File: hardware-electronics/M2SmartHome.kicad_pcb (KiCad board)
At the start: 4 copper layers, 22 x 76 mm, 208 parts, among them J1 M.2-Key-M-edge-connector, J3 CONMHF1-SMD-T, J4 CONMHF1-SMD-T, J5 Micro_SD_Card_Det_Hirose_DM3AT, U1 RTL8188FTV-VC-CG, U10 24AA04T-I_OT, U2 EMMC16G-MW28-01E10, U3 PI7C9X440SLBFDE, U4 24AA04T-I_OT, U5 CP2102N-A02-GQFN20, U6 24AA04T-I_OT, U7 EFR32MG21B020F1024IM32-B, U8 USB2244-AEZG-06, U9 USB2244-AEZG-06, Y1 ABM8-12.000MHZ-B2-T, Y2 ECS-240-10-47-CKM-TR, Y3 ECS-240-10-47-CKM-TR, Y4 ABM8-38.400MHZ-10-D1G-T, Y5 ABM8-40.000MHZ-B2-T

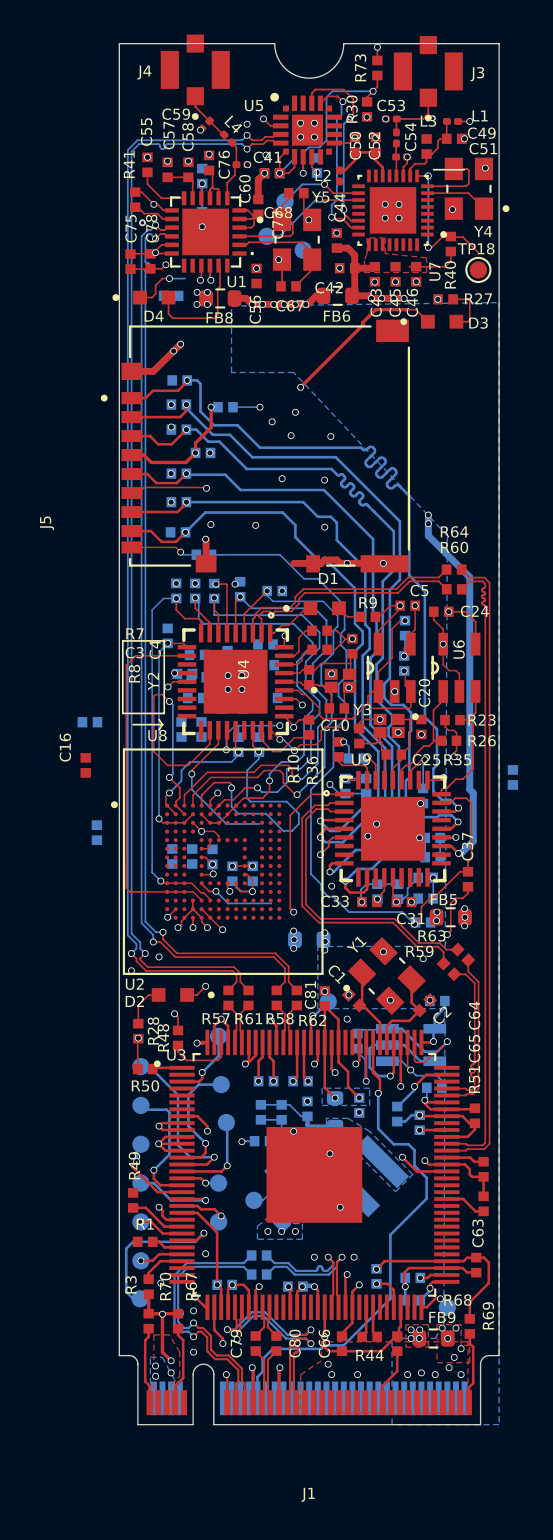
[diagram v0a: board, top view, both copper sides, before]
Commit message: [#17] eMMC routing WIP
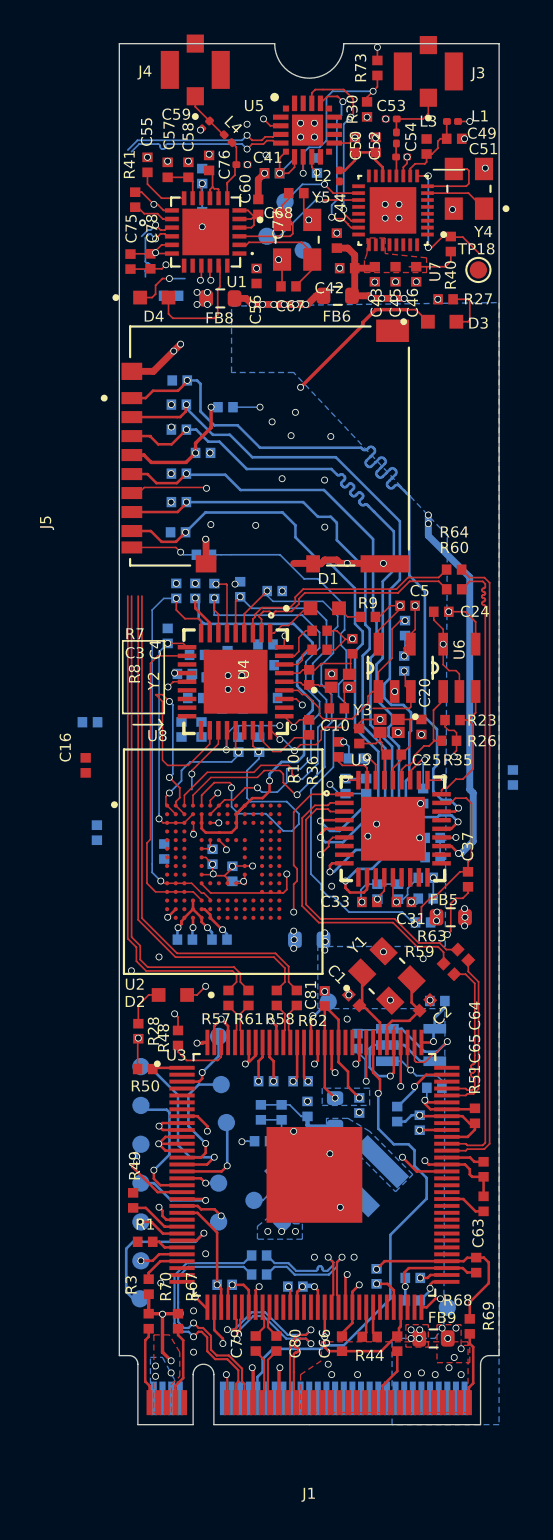
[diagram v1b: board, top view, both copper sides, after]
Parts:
- moved C15 5.07 mm to (86.8, 137.9), turned to 180 degrees
- moved C23 5.05 mm to (84.8, 137.9), turned to 180 degrees
- moved C19 2.53 mm to (86.4, 133.1), turned to 90 degrees
- moved C22 0.55 mm to (83.6, 132.8)
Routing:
- net /pcie-usb-bridge/USB_3_DP: track 64.1 -> 38.1 mm, vias 2 -> 1
- net /pcie-usb-bridge/USB_3_DN: track 64.1 -> 38.1 mm, vias 2 -> 1
- net /pcie-usb-bridge/USB_4_DP: track 53.1 -> 32.1 mm, vias 2 -> 1
- net /pcie-usb-bridge/USB_4_DN: track 53.1 -> 34.4 mm, vias 2 -> 1
- net Net-(U2-RST_N): track 13.3 -> 10.2 mm
- net Net-(U2-CMD): track 21.3 -> 18.7 mm
- net GND: track 159.8 -> 162.1 mm
- net Net-(U2-DAT6): track 26.7 -> 28.7 mm
- net +3V3_eMMC: track 25.4 -> 24.6 mm, vias 17 -> 19
- removed copper zone on In2.Cu, net (none)

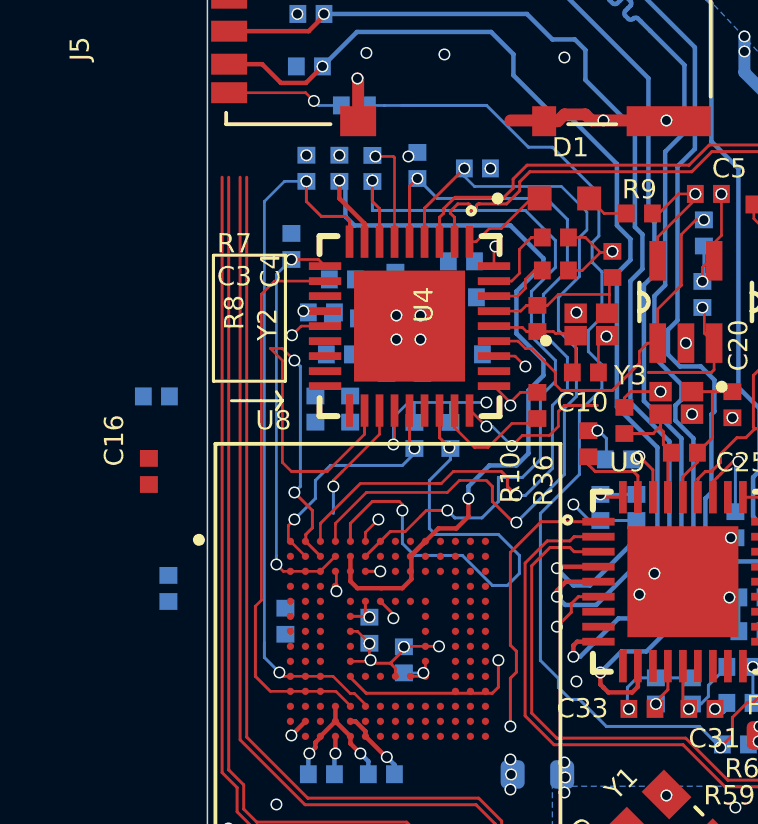
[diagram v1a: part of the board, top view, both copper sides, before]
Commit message: [#17] eMMC routing WIP
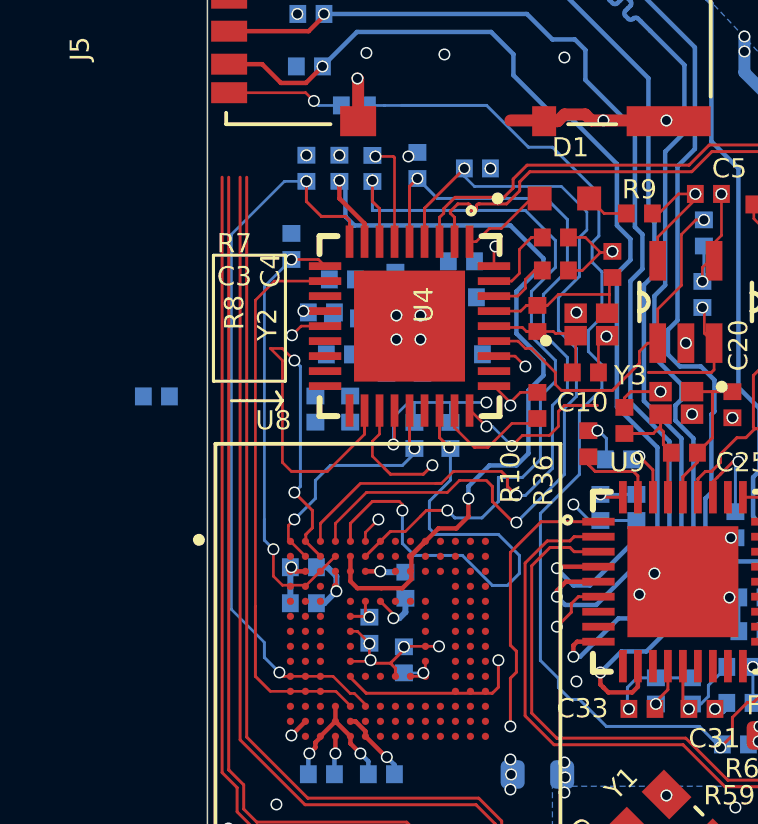
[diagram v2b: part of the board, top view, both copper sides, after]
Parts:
- C16: moved to B.Cu
- moved C16 9.35 mm to (87.6, 131.6)
- moved C21 4.53 mm to (84.2, 132.2), turned to 180 degrees
- moved C22 1.90 mm to (84.2, 131.0), turned to 180 degrees
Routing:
- net GND: track 162.1 -> 165.2 mm
- net Net-(U2-VDDI): track 0.00 -> 1.72 mm, vias 0 -> 1
- net Net-(U2-DAT5): track 13.9 -> 14.9 mm
- net Net-(U2-CLK): track 24.0 -> 24.9 mm
- net +3V3_eMMC: track 24.6 -> 25.5 mm

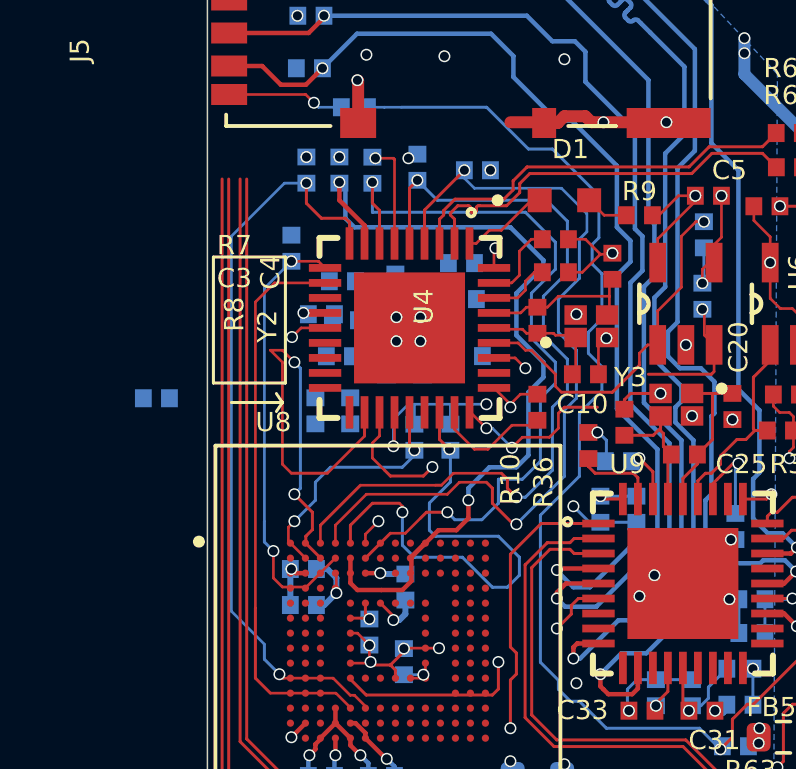
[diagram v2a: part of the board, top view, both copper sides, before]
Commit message: [#17] eMMC routing WIP
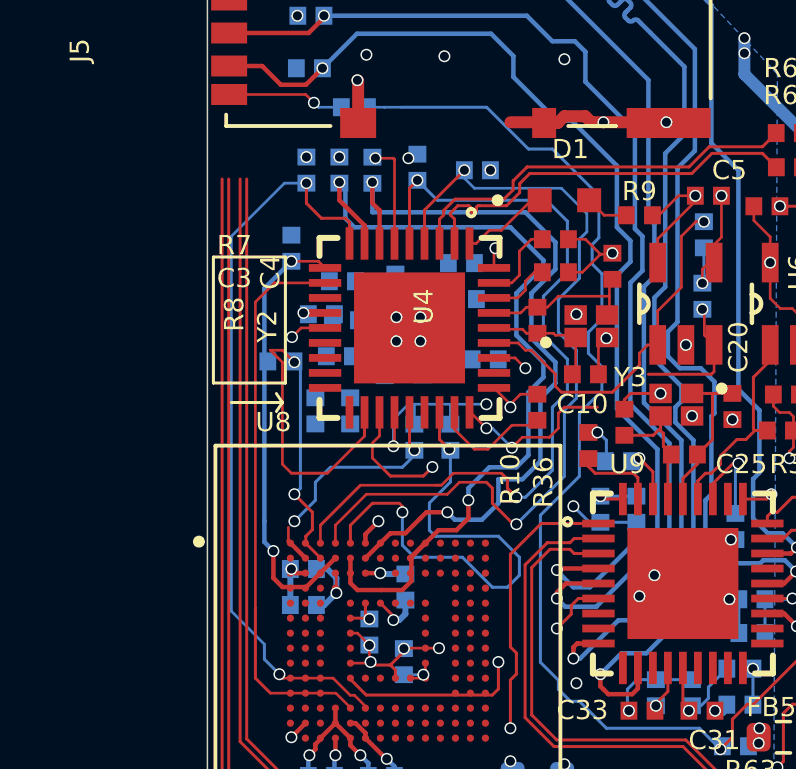
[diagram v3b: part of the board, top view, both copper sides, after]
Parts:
- moved R15 4.33 mm to (83.5, 124.1), turned to 180 degrees
- moved R4 0.54 mm to (90.3, 124.0)
- moved C17 0.06 mm to (86.9, 124.1)
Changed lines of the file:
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@@
 			(outputformat 1)
 			(mirror no)
-			(drillshape 1)
+			(drillshape 0)
 			(scaleselection 1)
 			(outputdirectory "")
@@
 	(footprint "M2SmartHomeFootprints:R_0402"
 		(layer "B.Cu")
-		(at 89.7325 123.9025)
+		(at 90.26 124.01)
 		(property "Reference" "R4"
 			(at 1.6675 0.005 0)
@@
 	(footprint "M2SmartHomeFootprints:C_0402"
 		(layer "B.Cu")
-		(at 86.9675 124.1025 -90)
+		(at 86.91 124.12 -90)
 		(property "Reference" "C17"
 			(at 1.905 -0.0325 90)
@@
 	(footprint "M2SmartHomeFootprints:R_0402"
 		(layer "B.Cu")
-		(at 79.3 125.3075)
+		(at 83.45 124.08 180)
 		(property "Reference" "R15"
 			(at 1.032 1.1564 0)
@@
 		)
 		(property "Footprint" "M2SmartHomeFootprints:R_0402"
-			(at 0 0 180)
+			(at 0 0 0)
 			(unlocked yes)
 			(layer "B.Fab")
@@
 		)
 		(property "Datasheet" "https://www.vishay.com/docs/20035/crcw0402.pdf"
-			(at 0 0 180)
+			(at 0 0 0)
 			(unlocked yes)
 			(layer "B.Fab")
@@
 		)
 		(property "Description" "SMD Thick Film Resistor, 49.9 kΩ, ±1%, 1/16 W, 0402 [1005 Metric], CRCW Series"
-			(at 0 0 180)
+			(at 0 0 0)
 			(unlocked yes)
 			(layer "B.Fab")
@@
 		)
 		(property "MPN" "CRCW040249K9FKED"
-			(at 0 0 180)
+			(at 0 0 0)
 			(unlocked yes)
 			(layer "B.Fab")
@@
 		)
 		(property "Manufacturer" "Vishay"
-			(at 0 0 180)
+			(at 0 0 0)
 			(unlocked yes)
 			(layer "B.Fab")
@@
 		)
 		(property "License" "Apache-2.0"
-			(at 0 0 180)
+			(at 0 0 0)
 			(unlocked yes)
 			(layer "B.Fab")
@@
 		)
 		(property "Author" "Your Name"
-			(at 0 0 180)
+			(at 0 0 0)
 			(unlocked yes)
 			(layer "B.Fab")
@@
 		)
 		(property "Val" "49k9"
-			(at 0 0 180)
+			(at 0 0 0)
 			(unlocked yes)
 			(layer "B.Fab")
@@
 		)
 		(property "Tolerance" "1%"
-			(at 0 0 180)
+			(at 0 0 0)
 			(unlocked yes)
 			(layer "B.Fab")
@@
 		)
 		(property "Power" "1/16 W"
-			(at 0 0 180)
+			(at 0 0 0)
 			(unlocked yes)
 			(layer "B.Fab")
@@
 		(attr smd)
 		(fp_line
-			(start -0.965 -0.55)
-			(end 0.965 -0.55)
+			(start 0.965 0.55)
+			(end -0.965 0.55)
 			(stroke
 				(width 0.05)
@@
 		)
 		(fp_line
-			(start -0.965 0.55)
-			(end -0.965 -0.55)
+			(start 0.965 -0.55)
+			(end 0.965 0.55)
 			(stroke
 				(width 0.05)
@@
 		)
 		(fp_line
-			(start 0.965 -0.55)
-			(end 0.965 0.55)
+			(start -0.965 0.55)
+			(end -0.965 -0.55)
 			(stroke
 				(width 0.05)
@@
 		)
 		(fp_line
-			(start 0.965 0.55)
-			(end -0.965 0.55)
+			(start -0.965 -0.55)
+			(end 0.965 -0.55)
 			(stroke
 				(width 0.05)
@@
 		)
 		(fp_line
-			(start -0.5 -0.25)
-			(end 0.5 -0.25)
+			(start 0.5 0.25)
+			(end -0.5 0.25)
 			(stroke
 				(width 0.127)
@@
 		)
 		(fp_line
-			(start -0.5 0.25)
-			(end -0.5 -0.25)
+			(start 0.5 -0.25)
+			(end 0.5 0.25)
 			(stroke
 				(width 0.127)
@@
 		)
 		(fp_line
-			(start 0.5 -0.25)
-			(end 0.5 0.25)
+			(start -0.5 0.25)
+			(end -0.5 -0.25)
 			(stroke
 				(width 0.127)
@@
 		)
 		(fp_line
-			(start 0.5 0.25)
-			(end -0.5 0.25)
+			(start -0.5 -0.25)
+			(end 0.5 -0.25)
 			(stroke
 				(width 0.127)
@@
 		)
 		(pad "1" smd rect
-			(at -0.434999 0)
+			(at -0.434999 0 180)
 			(size 0.56 0.6)
 			(layers "B.Cu" "B.Paste" "B.Mask")
@@
 		)
 		(pad "2" smd rect
-			(at 0.434999 0)
+			(at 0.434999 0 180)
 			(size 0.56 0.6)
 			(layers "B.Cu" "B.Paste" "B.Mask")
@@
 		(start 86.7 129.4075)
 		(end 86.2675 129.84)
-		(width 0.09)
+		(width 0.15)
 		(layer "F.Cu")
 		(net 1)
@@
 		(start 86.2675 129.84)
 		(end 86.2675 130.1375)
-		(width 0.09)
+		(width 0.15)
 		(layer "F.Cu")
 		(net 1)
@@
 	)
 	(segment
-		(start 83.9 129.4075)
-		(end 83.7 129.6075)
-		(width 0.09)
-		(layer "F.Cu")
-		(net 131)
-	)
-	(segment
 		(start 84.2675 130.635)
 		(end 84.2675 130.6375)
@@
 		(start 83.7 130.0675)
 		(end 84.2675 130.635)
-		(width 0.09)
+		(width 0.15)
 		(layer "F.Cu")
 		(net 131)
@@
 		(start 83.2 130.4)
 		(end 83.2 131.3)
-		(width 0.09)
+		(width 0.15)
 		(layer "F.Cu")
 		(net 133)
@@
 		(start 83.2 131.3)
 		(end 83.5 131.6)
-		(width 0.09)
+		(width 0.15)
 		(layer "F.Cu")
 		(net 133)
@@
 		(start 84.2975 131.6)
 		(end 85.26 130.6375)
-		(width 0.09)
+		(width 0.15)
 		(layer "F.Cu")
 		(net 133)
@@
 		(start 83.5 131.6)
 		(end 84.2975 131.6)
-		(width 0.09)
+		(width 0.15)
 		(layer "F.Cu")
 		(net 133)
@@
 		(start 85.26 130.6375)
 		(end 85.2675 130.6375)
-		(width 0.09)
+		(width 0.15)
 		(layer "F.Cu")
 		(net 133)
@@
 		(start 83.2 130.4)
 		(end 82.9 130.1)
-		(width 0.1)
+		(width 0.15)
 		(layer "B.Cu")
 		(net 133)
@@
 		(start 82.9 130.1)
 		(end 82.9 129.4)
-		(width 0.1)
+		(width 0.15)
 		(layer "B.Cu")
 		(net 133)
@@
 		(start 82.9 129.4)
 		(end 82.9 121.642499)
-		(width 0.09)
+		(width 0.15)
 		(layer "B.Cu")
 		(net 133)
@@
 		(start 82.9 121.642499)
 		(end 83.8 120.742499)
-		(width 0.09)
+		(width 0.15)
 		(layer "B.Cu")
 		(net 133)
@@
 		(start 88.3 129.1075)
 		(end 88.1 129.3075)
-		(width 0.1)
+		(width 0.15)
 		(layer "F.Cu")
 		(net 135)
@@
 		(start 86.7375 119.045)
 		(end 86.7375 120.14775)
-		(width 0.1)
+		(width 0.15)
 		(layer "F.Cu")
 		(net 135)
@@
 		(start 87.1 129.8075)
 		(end 87.09875 129.80625)
-		(width 0.09)
+		(width 0.15)
 		(layer "F.Cu")
 		(net 135)
@@
 		(start 88.1 129.3075)
 		(end 87.6 129.8075)
-		(width 0.09)
+		(width 0.15)
 		(layer "F.Cu")
 		(net 135)
@@
 		(start 89 129.1075)
 		(end 88.3 129.1075)
-		(width 0.1)
+		(width 0.15)
 		(layer "F.Cu")
 		(net 135)
@@
 		(start 86.5 118.1075)
 		(end 86.5 118.8075)
-		(width 0.1)
+		(width 0.15)
 		(layer "F.Cu")
 		(net 135)
@@
 		(start 86.5 118.8075)
 		(end 86.7375 119.045)
-		(width 0.1)
+		(width 0.15)
 		(layer "F.Cu")
 		(net 135)
@@
 		(start 87.09875 129.80625)
 		(end 86.29125 130.61375)
-		(width 0.1)
+		(width 0.15)
 		(layer "F.Cu")
 		(net 135)
@@
 		(start 87.6 129.8075)
 		(end 87.1 129.8075)
-		(width 0.09)
+		(width 0.15)
 		(layer "F.Cu")
 		(net 135)
@@
 		(start 86.29125 130.61375)
 		(end 86.29125 130.63875)
-		(width 0.1)
+		(width 0.15)
 		(layer "F.Cu")
 		(net 135)
@@
 		(start 90.7 128.8075)
 		(end 90.15 129.3575)
-		(width 0.1)
+		(width 0.15)
 		(layer "B.Cu")
 		(net 135)
@@
 		(start 91.8 123.3075)
 		(end 92.6 124.1075)
-		(width 0.1)
+		(width 0.15)
 		(layer "B.Cu")
 		(net 135)
@@
 		(start 90.15 129.3575)
 		(end 89.25 129.3575)
-		(width 0.1)
+		(width 0.15)
 		(layer "B.Cu")
 		(net 135)
@@
 		(start 91.5 128.0075)
 		(end 90.7 128.0075)
-		(width 0.1)
+		(width 0.15)
 		(layer "B.Cu")
 		(net 135)
@@
 		(start 92.1 127.4075)
 		(end 91.5 128.0075)
-		(width 0.1)
+		(width 0.15)
 		(layer "B.Cu")
 		(net 135)
@@
 		(start 86.5 119.1075)
 		(end 91.6 119.1075)
-		(width 0.1)
+		(width 0.15)
 		(layer "B.Cu")
 		(net 135)
@@
 		(start 90.7 128.0075)
 		(end 90.7 128.8075)
-		(width 0.1)
+		(width 0.15)
 		(layer "B.Cu")
 		(net 135)
@@
 		(start 92.6 124.1075)
 		(end 92.6 124.8075)
-		(width 0.1)
+		(width 0.15)
 		(layer "B.Cu")
 		(net 135)
@@
 		(start 92.6 120.1075)
 		(end 92.6 121.0075)
-		(width 0.1)
+		(width 0.15)
 		(layer "B.Cu")
 		(net 135)
@@
 		(start 91.6 119.1075)
 		(end 92.6 120.1075)
-		(width 0.1)
+		(width 0.15)
 		(layer "B.Cu")
 		(net 135)
@@
 		(start 92.6 121.0075)
 		(end 91.8 121.8075)
-		(width 0.1)
+		(width 0.15)
 		(layer "B.Cu")
 		(net 135)
@@
 		(start 89.25 129.3575)
 		(end 89 129.1075)
-		(width 0.1)
+		(width 0.15)
 		(layer "B.Cu")
 		(net 135)
@@
 		(start 92.6 124.8075)
 		(end 92.1 125.3075)
-		(width 0.1)
+		(width 0.15)
 		(layer "B.Cu")
 		(net 135)
@@
 		(start 86.5 118.1075)
 		(end 86.5 119.1075)
-		(width 0.1)
+		(width 0.15)
 		(layer "B.Cu")
 		(net 135)
@@
 		(start 91.8 121.8075)
 		(end 91.8 123.3075)
-		(width 0.1)
+		(width 0.15)
 		(layer "B.Cu")
 		(net 135)
@@
 		(start 92.1 125.3075)
 		(end 92.1 127.4075)
-		(width 0.1)
+		(width 0.15)
 		(layer "B.Cu")
 		(net 135)

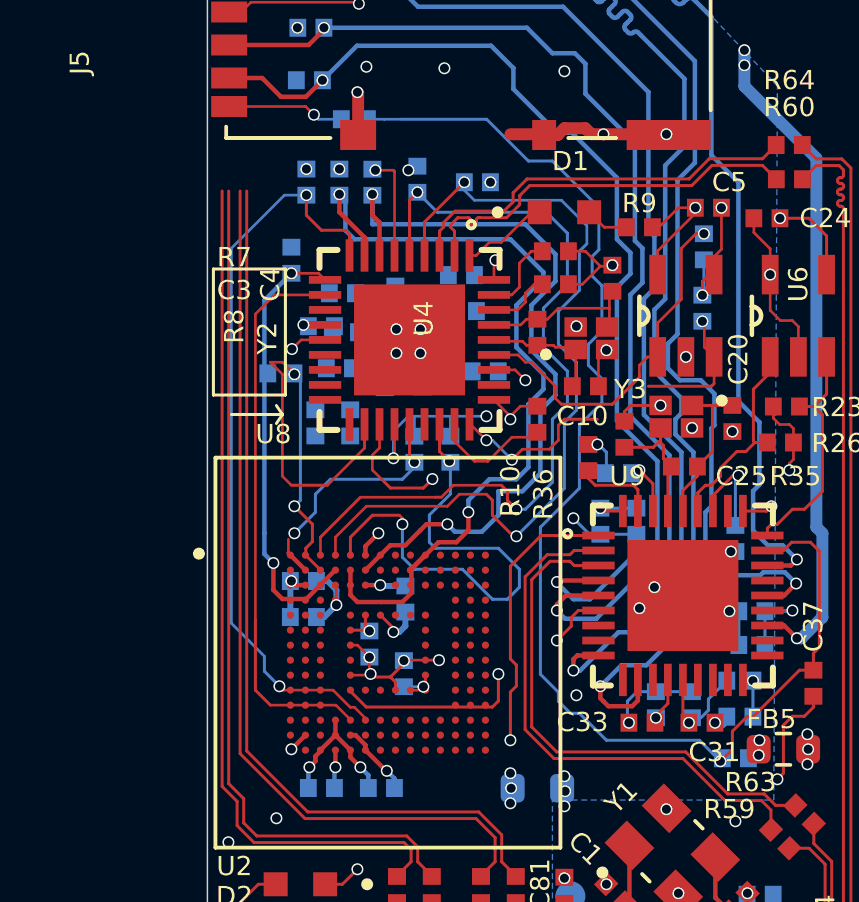
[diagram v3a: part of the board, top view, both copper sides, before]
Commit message: [#17] eMMC routing WIP set proper trace wthicknes to keep SE 50 ohm
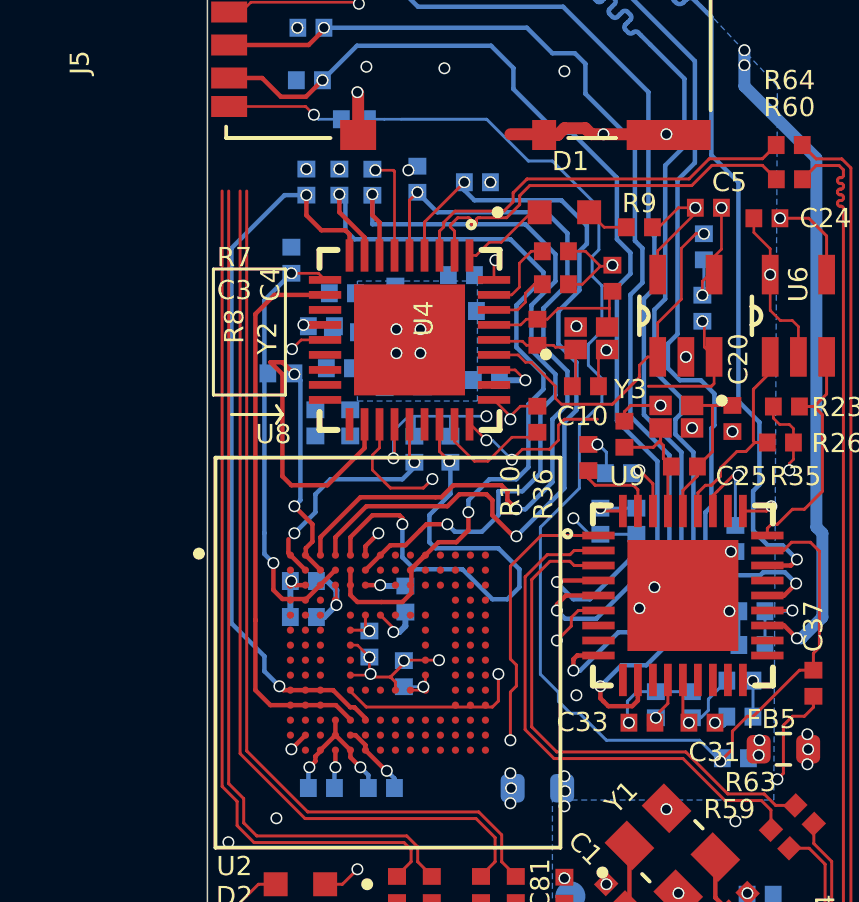
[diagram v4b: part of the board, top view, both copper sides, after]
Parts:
- moved R4 0.29 mm to (90.3, 124.3)
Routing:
- net Net-(U8-SD_WP): track 1.19 -> 2.06 mm
- added copper zone on B.Cu, net GND
